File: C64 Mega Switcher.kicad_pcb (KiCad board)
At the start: 2 copper layers, 79.8 x 75.6 mm, 20 parts, among them J1 Port 1, J2 Port 2, J3 Mega Drive, J4 C_SEL, J5 B_SEL, SW1 P1_SEL, SW2 P2_SEL, U1 4053, U2 4053, U3 NE555

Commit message: General part placement
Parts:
- SW1, SW2: moved to B.Cu
- U1, U2: value 4053 -> 74HCT4053
- moved D1 107.5 mm to (113.7, 41.3), turned to 90 degrees
- moved C3 90.9 mm to (138.2, 46.5), turned to 270 degrees
- moved SW2 83.6 mm to (133.3, 105.4)
- moved SW1 82.6 mm to (133.3, 113.0)
- moved D2 79.5 mm to (113.7, 73.0), turned to 90 degrees
- moved J5 77.4 mm to (126.2, 78.2)
- moved R1 73.8 mm to (126.5, 58.2), turned to 270 degrees
- moved U3 54.0 mm to (126.5, 46.5)
- moved R2 50.2 mm to (130.3, 58.2), turned to 270 degrees
- moved JP1 49.1 mm to (126.2, 96.0), turned to 90 degrees
- moved R3 48.9 mm to (134.4, 58.2), turned to 270 degrees
- moved R4 48.0 mm to (138.2, 58.2), turned to 270 degrees
- moved U2 41.1 mm to (111.8, 78.2)
- moved J4 39.8 mm to (126.2, 87.1)
- moved C2 11.2 mm to (119.4, 74.3), turned to 90 degrees
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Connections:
- U1 pad 16: VDD -> VCC
- U1 pad 8: VSS -> GND
- U2 pad 16: VDD -> VCC
- U2 pad 8: VSS -> GND
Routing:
- added copper zone on B.Cu, net GND
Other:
- board size 79.8 x 75.6 mm -> 44.2 x 79.5 mm
- board text added: "Commodore 64 Mega Switcher"
- board text added: "Port 1"
- board text added: "Port 2"

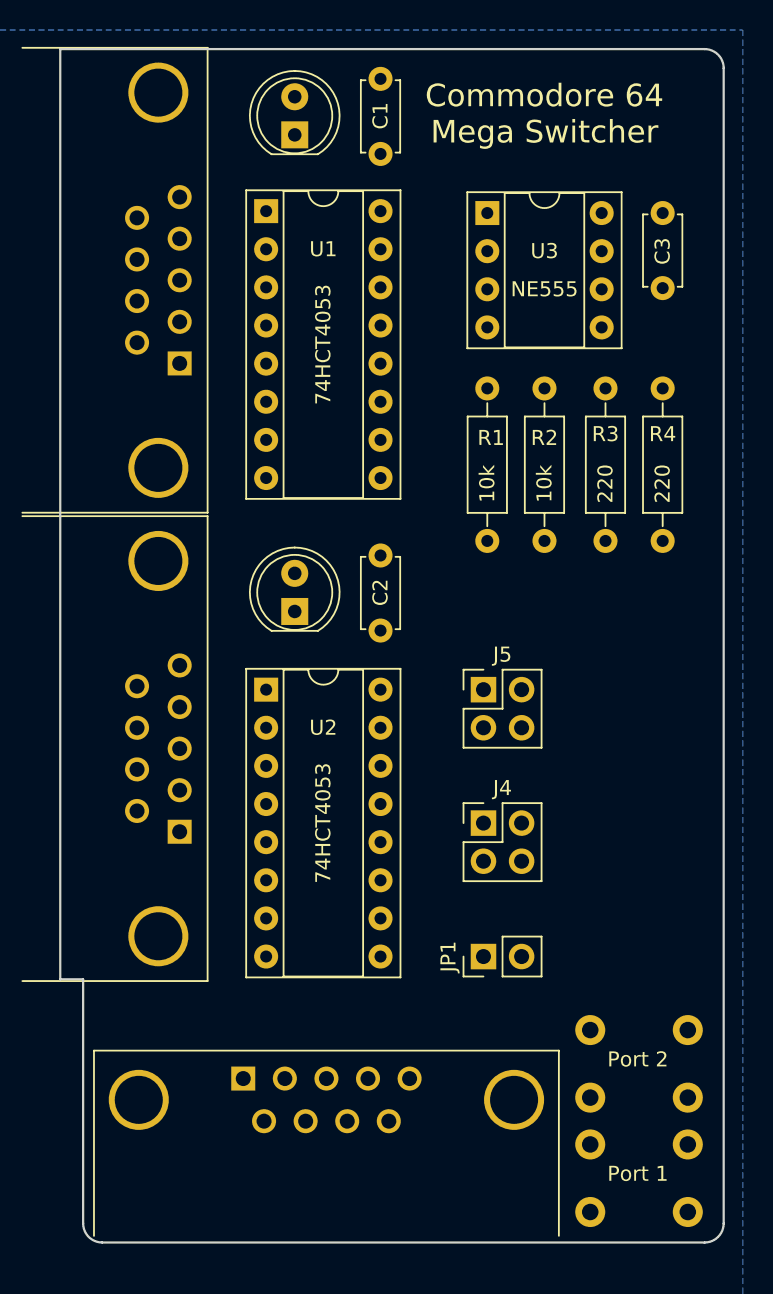
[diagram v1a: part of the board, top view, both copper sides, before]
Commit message: Routed nets and added silkscreen text
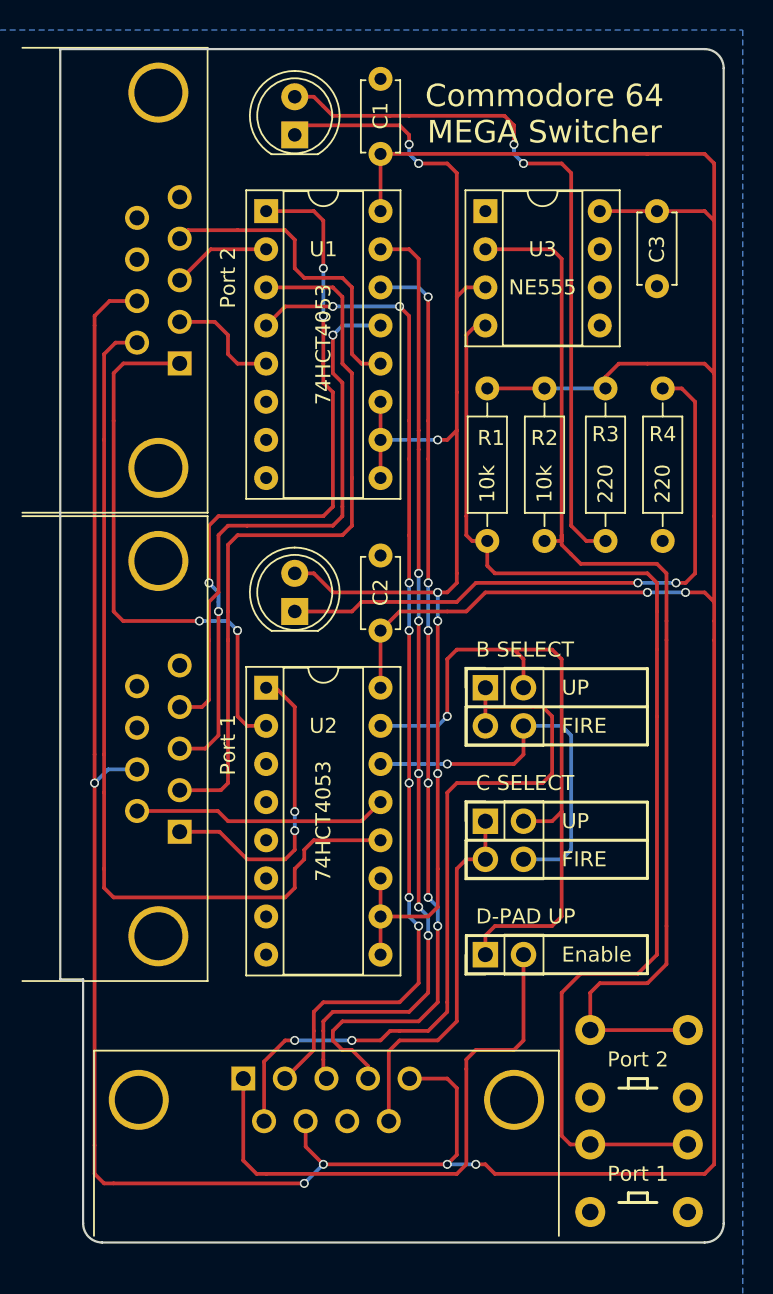
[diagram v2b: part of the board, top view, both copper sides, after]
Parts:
- moved C3 0.40 mm to (137.8, 46.4)
- moved U3 0.18 mm to (126.4, 46.4)
- moved J4 0.18 mm to (126.4, 87.0)
- moved J5 0.18 mm to (126.4, 78.1)
- moved JP1 0.18 mm to (126.4, 95.9)
- moved U2 0.13 mm to (111.8, 78.1)
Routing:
- net VCC: track 0.00 -> 263.0 mm, vias 0 -> 7
- net PORT: track 0.00 -> 94.7 mm, vias 0 -> 6
- net Net-(R1-Pad2): track 0.00 -> 80.2 mm
- net Net-(R2-Pad2): track 0.00 -> 74.6 mm
- net DOWN: track 0.00 -> 68.1 mm, vias 0 -> 7
- net LEFT: track 0.00 -> 63.6 mm, vias 0 -> 5
- net RIGHT: track 0.00 -> 63.0 mm, vias 0 -> 6
- net Net-(J2-Pad6): track 0.00 -> 60.1 mm
- net Net-(J3-Pad6): track 0.00 -> 50.7 mm, vias 0 -> 2
- net Net-(J1-Pad3): track 0.00 -> 49.3 mm, vias 0 -> 4
- net Net-(J1-Pad2): track 0.00 -> 48.9 mm
- net Net-(D1-Pad2): track 0.00 -> 47.8 mm, vias 0 -> 2
- net UP: track 0.00 -> 46.3 mm, vias 0 -> 1
- net Net-(D2-Pad1): track 0.00 -> 41.7 mm, vias 0 -> 2
- net /MD_U: track 0.00 -> 38.4 mm
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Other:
- board text added: "B SELECT"
- board text added: "C SELECT"
- board text added: "Commodore 64 MEGA Switcher"
- board text added: "D-PAD UP"
- board text added: "Enable"
- board text added: "FIRE"
- board text added: "Licensed under CERN OHL v.1.2"
- board text added: "UP"
- board text removed: "Commodore 64 Mega Switcher"
